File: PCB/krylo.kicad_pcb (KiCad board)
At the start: 2 copper layers, 135.3 x 87.6 mm, 52 parts, among them SW1 Switch, SW10 Switch, SW11 Switch, SW12 Switch, SW13 Switch, SW14 Switch, SW15 Switch, SW16 Switch, SW2 Switch, SW3 Switch, SW4 Switch, SW5 Switch, SW6 Switch, SW7 Switch, SW8 Switch, SW9 Switch, U1 nice_nano

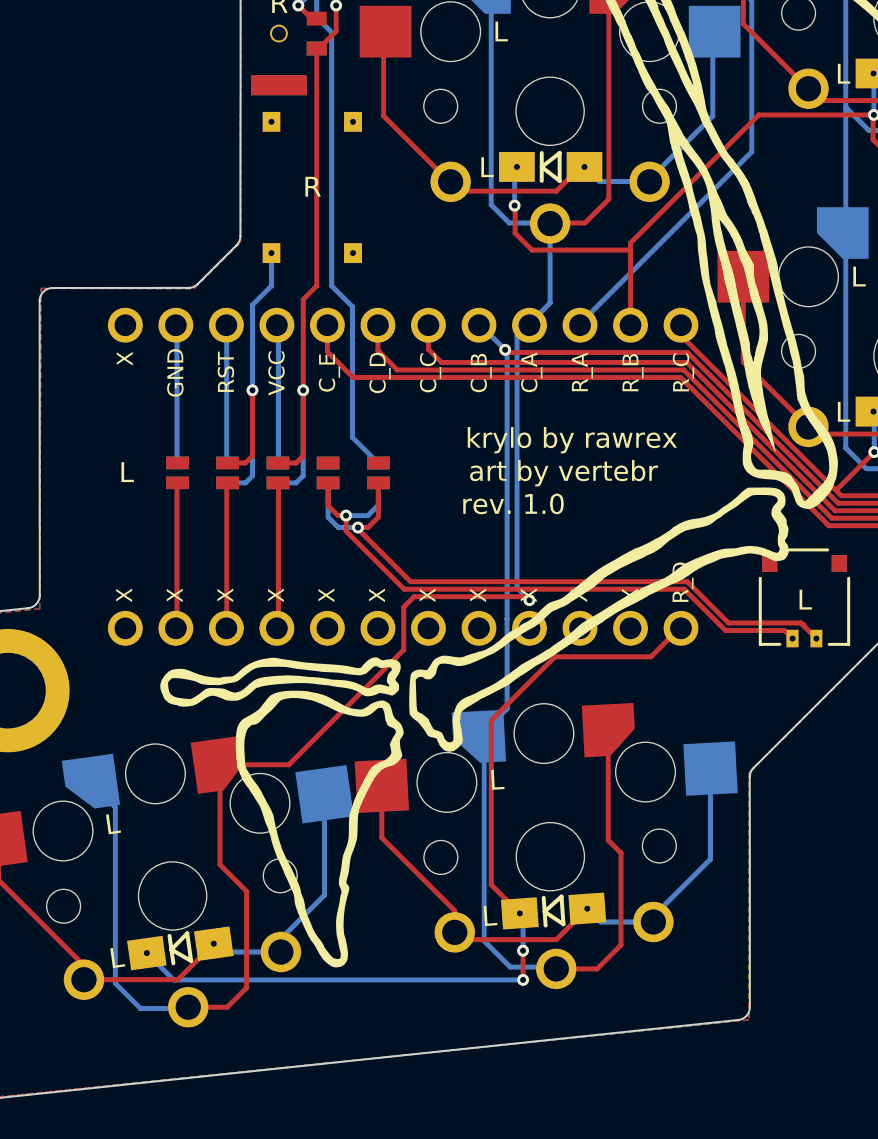
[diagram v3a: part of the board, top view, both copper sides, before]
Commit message: DRC clean up and stitching vias added
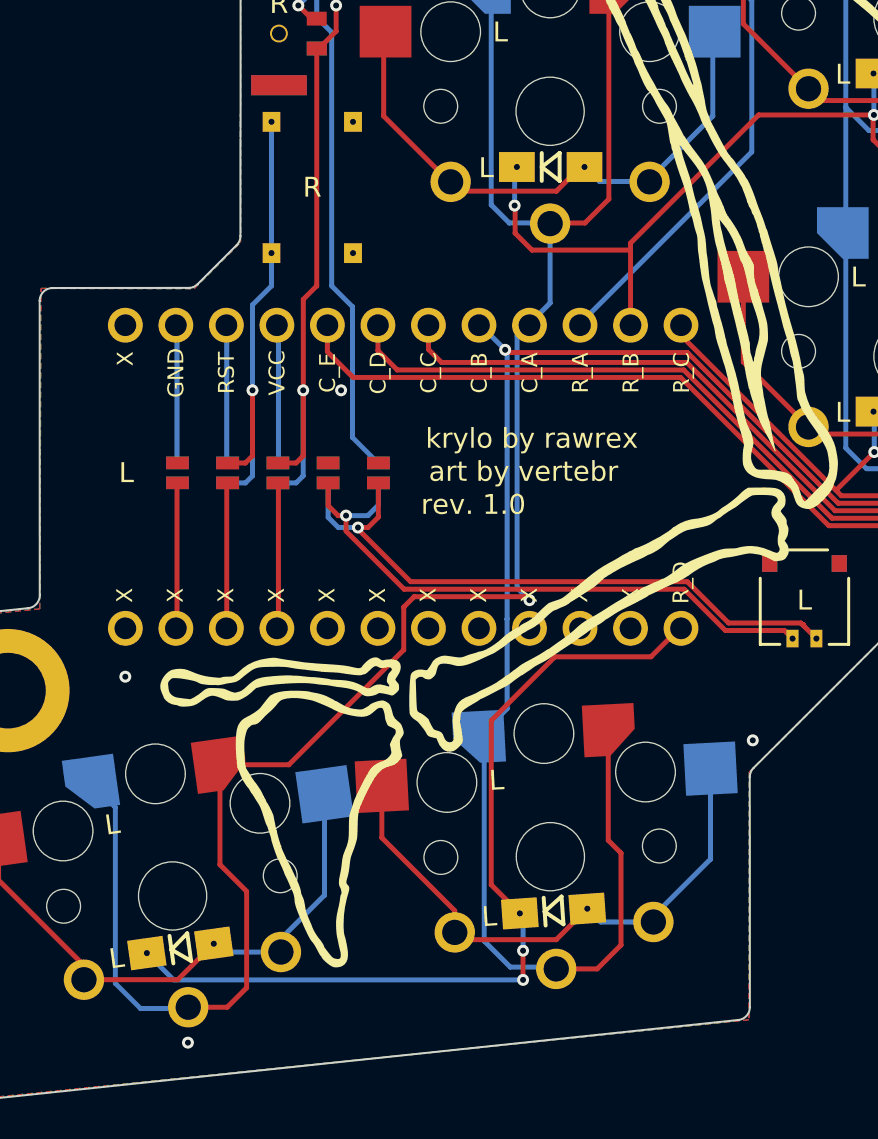
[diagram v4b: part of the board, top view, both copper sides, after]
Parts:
- BT1: value Molex -> MOLEX_C
- H1, H2, H3, H4: value SMTSO2020MTJ_M2 -> Mount
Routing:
- net RESET: track 17.7 -> 24.3 mm
- net GND: vias 0 -> 4
